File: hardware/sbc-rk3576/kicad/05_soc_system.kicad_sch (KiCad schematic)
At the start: 22 parts, among them J501 DEBUG UART, SW501 MASKROM, SW502 POWER, SW503 RESET, U401 RK3576, Y501 24MHz

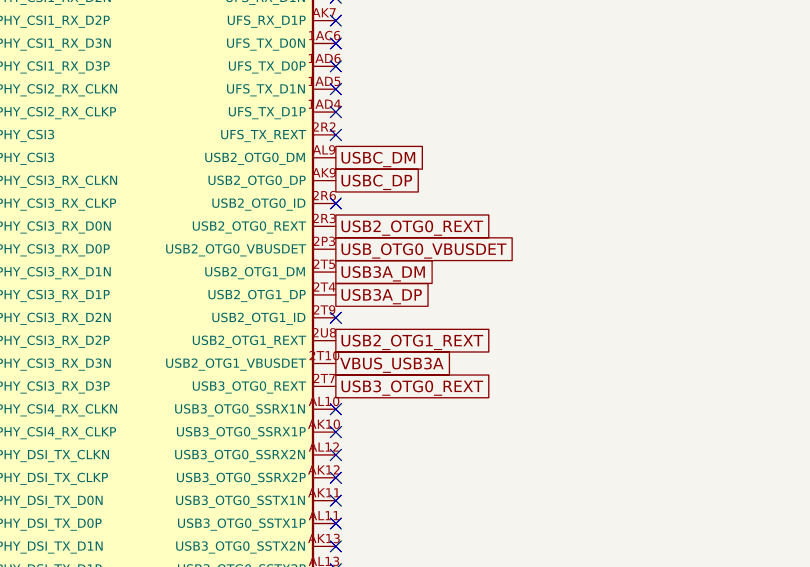
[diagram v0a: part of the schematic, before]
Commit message: hardware: add GbE, USB hub + 2x USB-A, Wi-Fi5/BT; real RK3576 land pattern; 100x72 board
- RK3576 footprint from LCSC C42388007 (all 698 ball IDs verified against the
  datasheet) replaces the placeholder.
- RTL8211F-CG RGMII PHY + HR911130C MagJack, FE1.1s 4-port hub (pinout per
  Terminus datasheet), stacked dual USB-A, BL-M8821CU1 Wi-Fi 5/BT 4.2 + u.FL.
- LCSC footprints get pad-derived courtyards; RJ45 pegs become NPTH.
- ERC 0/0, DRC 0 violations, parity 0 (placement stage).

Co-Authored-By: Claude Opus 5.5 <noreply@anthropic.com>
Claude-Session: https://claude.ai/code/session_01DP7VBm9fUdwhcDWq3gWKJ6
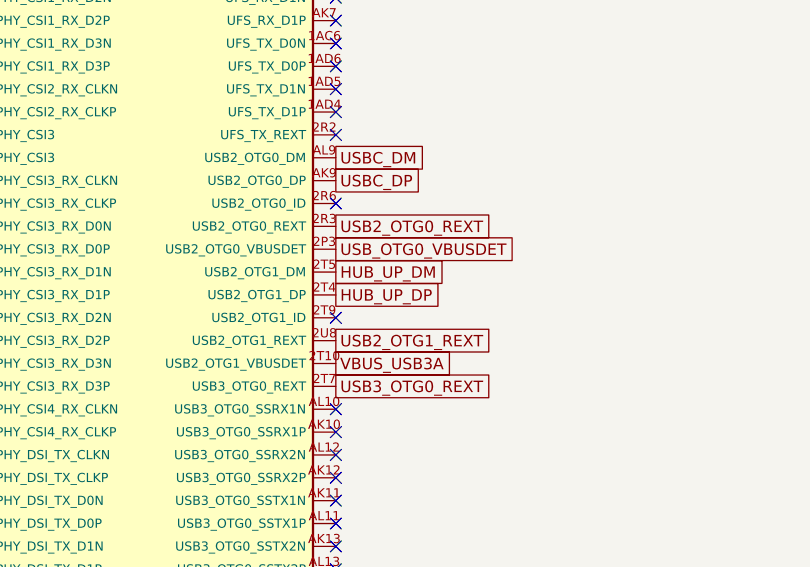
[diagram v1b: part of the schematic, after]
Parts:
- U401: footprint sbc:RK3576_FCCSP-698_16.1x17.2mm_PLACEHOLDER -> sbc:RK3576_FCCSP-698_16.1x17.2mm
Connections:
- net USB3A_DM renamed HUB_UP_DM
- net USB3A_DP renamed HUB_UP_DP
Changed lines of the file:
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@@
     (property "Reference" "U401" (at 60.96 33.02 0) (effects (font (size 1.27 1.27))))
     (property "Value" "RK3576" (at 60.96 187.96 0) (effects (font (size 1.27 1.27))))
-    (property "Footprint" "sbc:RK3576_FCCSP-698_16.1x17.2mm_PLACEHOLDER"
+    (property "Footprint" "sbc:RK3576_FCCSP-698_16.1x17.2mm"
       (at 60.96 109.22 0)
       (effects (font (size 1.27 1.27)) hide)
@@
     )
   )
-  (global_label "USB3A_DM"
+  (global_label "HUB_UP_DM"
     (shape passive)
     (at 83.82 149.86 0)
@@
     )
   )
-  (global_label "USB3A_DP"
+  (global_label "HUB_UP_DP"
     (shape passive)
     (at 83.82 152.4 0)
